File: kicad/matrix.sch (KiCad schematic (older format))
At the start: 19 parts, among them U1 TLC59025, U2 74HC595, U3 74HC595

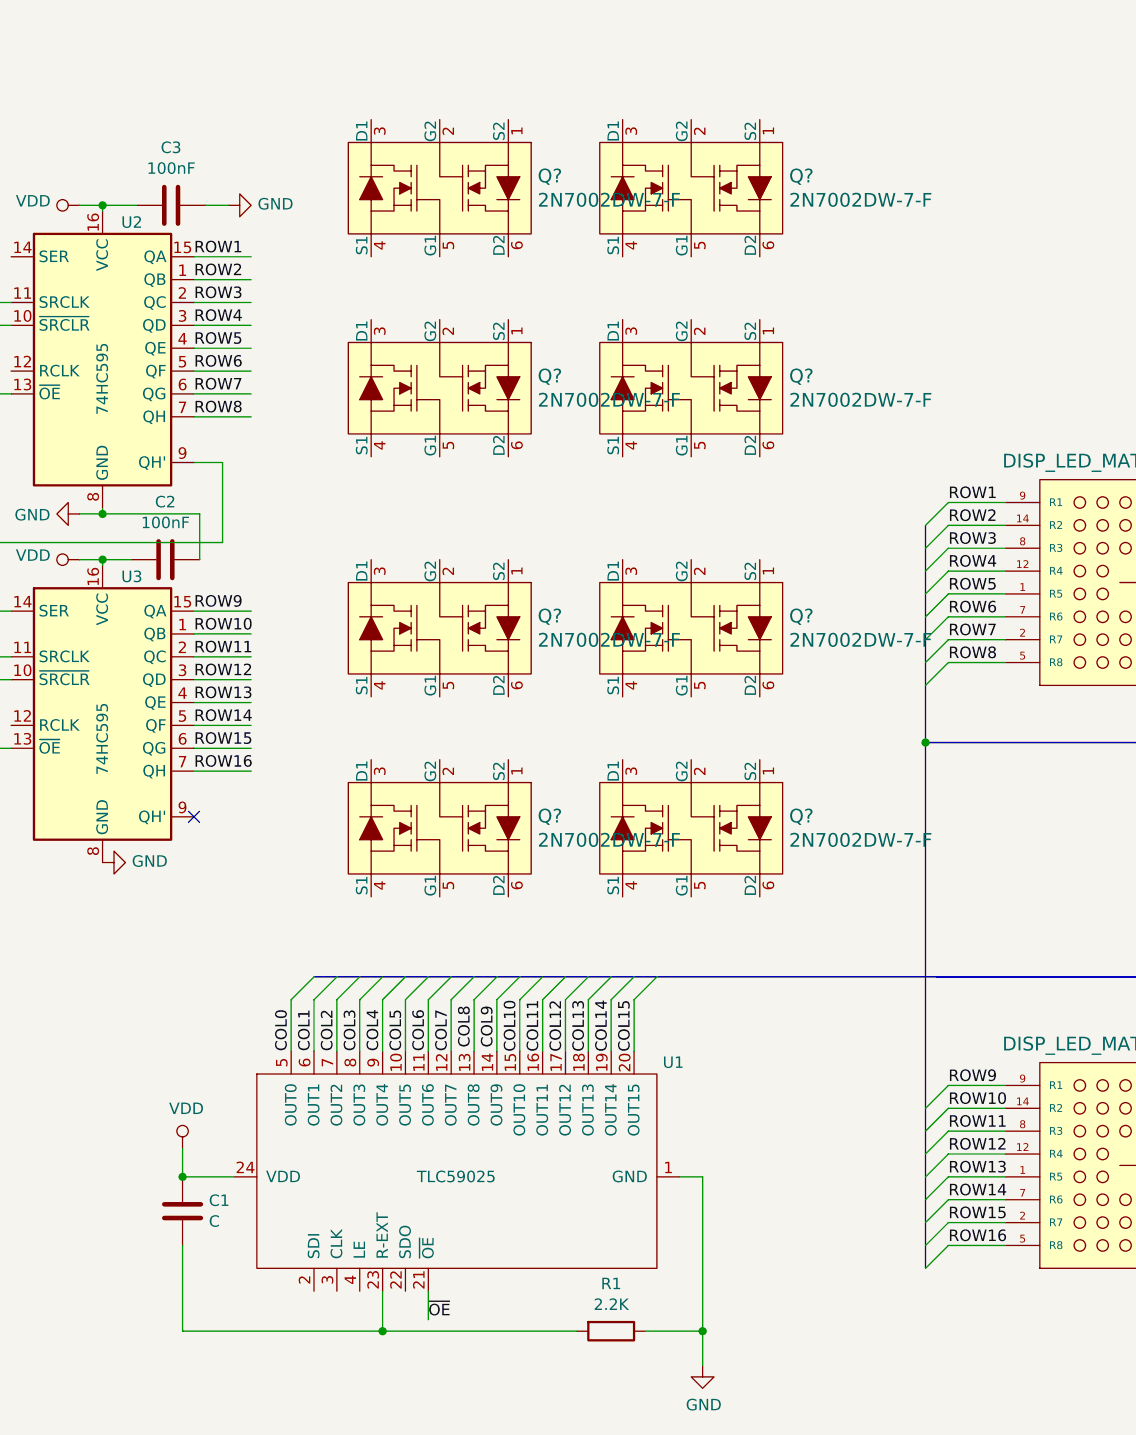
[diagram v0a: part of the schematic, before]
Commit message: Add footprints and initial layout
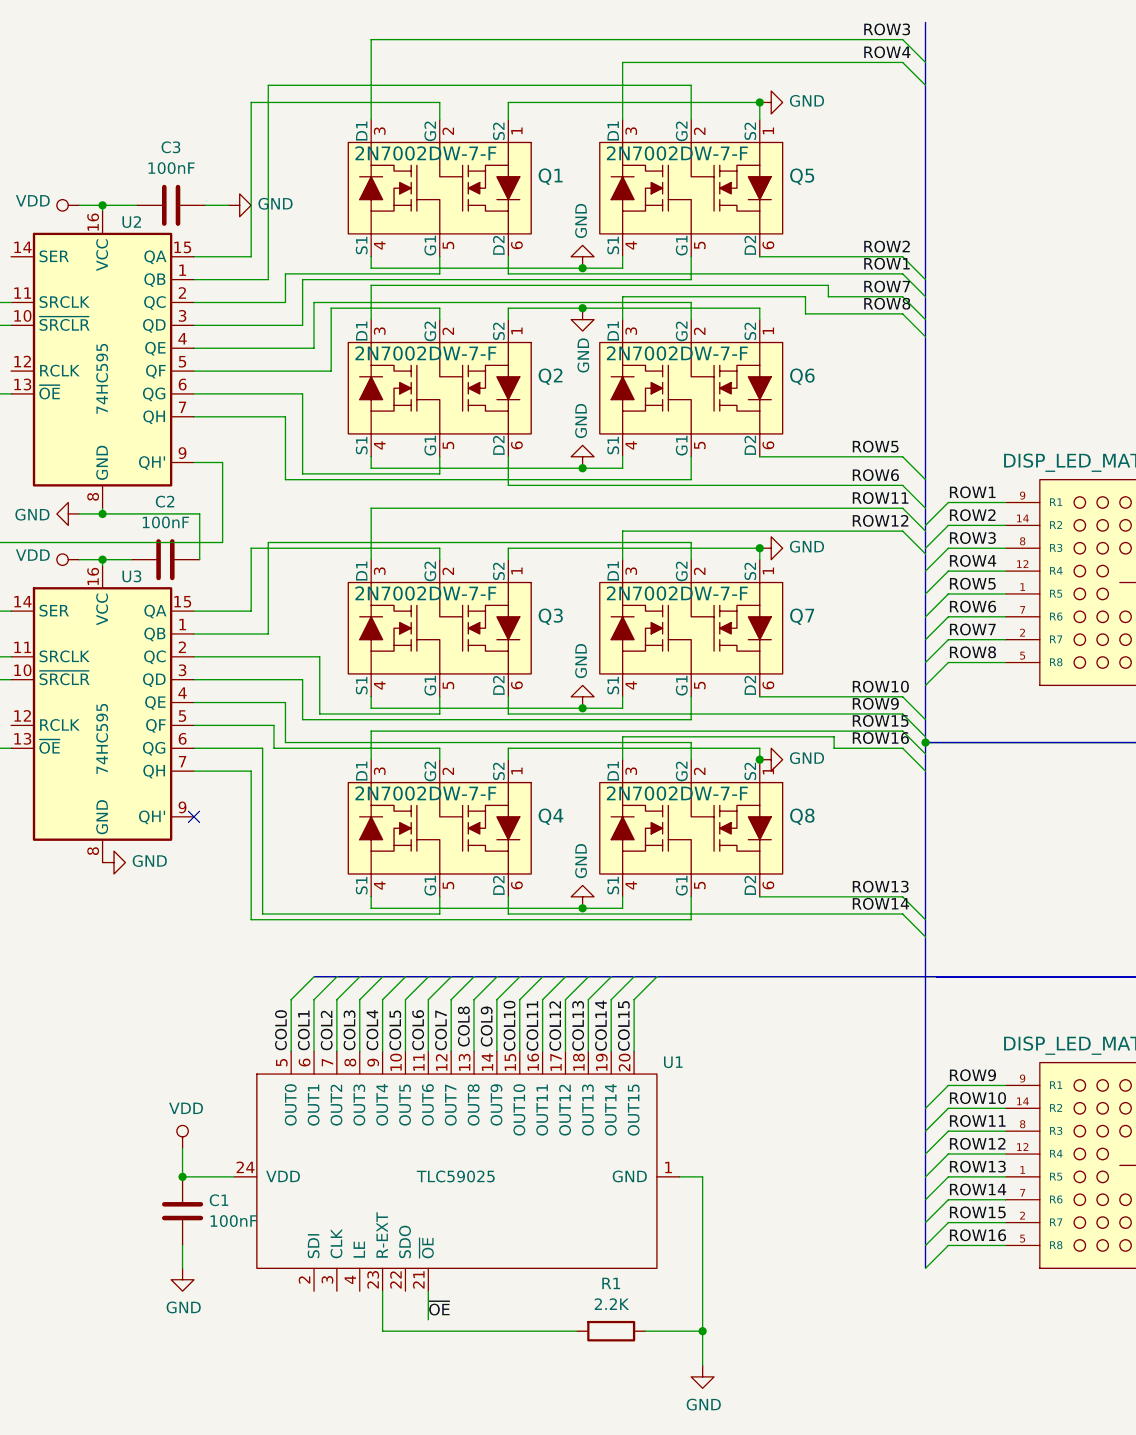
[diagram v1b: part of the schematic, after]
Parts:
- C1: value C -> 100nF; footprint (none) -> Capacitor_SMD:C_0805_2012Metric_Pad1.15x1.40mm_HandSolder
- C2, C3: footprint (none) -> Capacitor_SMD:C_0805_2012Metric_Pad1.15x1.40mm_HandSolder
- R1: footprint (none) -> Resistor_SMD:R_1206_3216Metric_Pad1.42x1.75mm_HandSolder
- gave numbers to parts that had none: 8
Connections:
- wire segments 132 -> 242

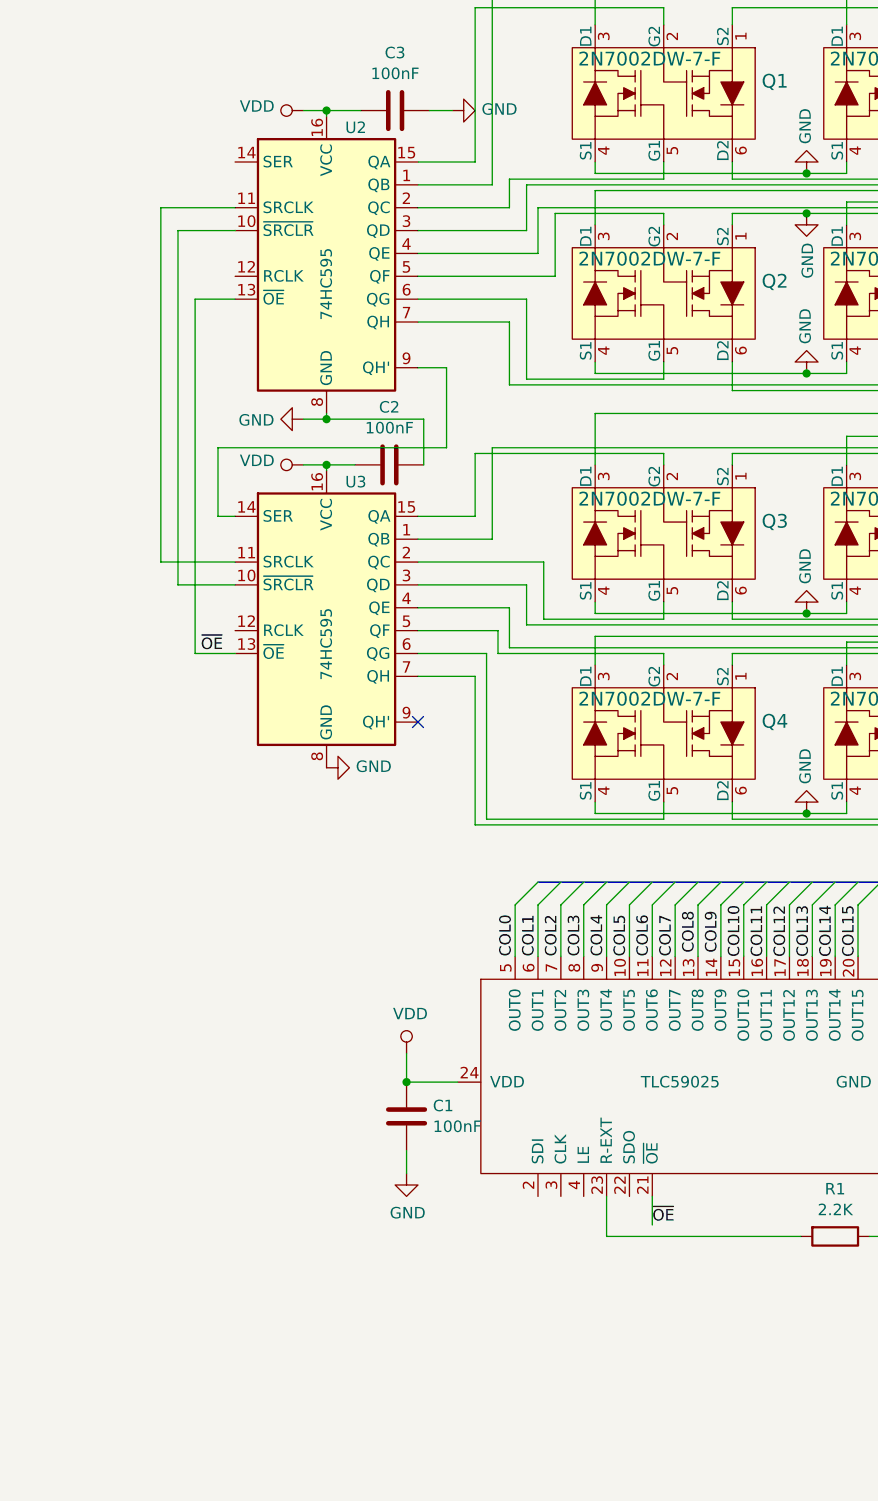
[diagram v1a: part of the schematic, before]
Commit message: Add headers to schematic
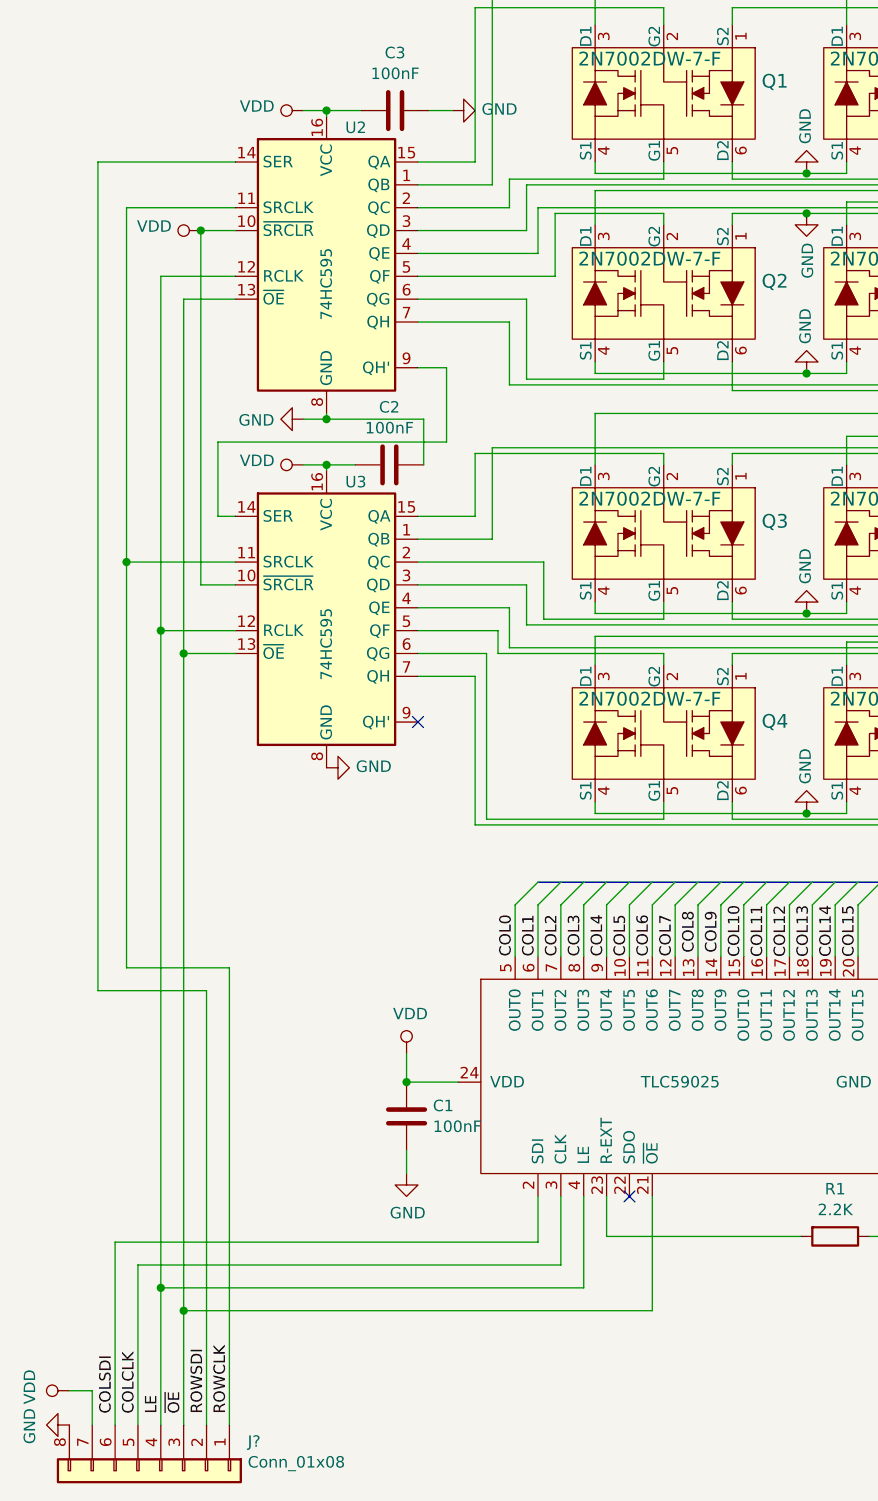
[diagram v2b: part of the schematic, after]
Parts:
- added J?: Conn_01x08, symbol Connector_Generic:Conn_01x08
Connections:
- net GND: now also J?.8 (Pin_8)
- net VDD: now also U2.10 (~SRCLR), U3.10 (~SRCLR), J?.7 (Pin_7)
- net ~OE: now also J?.3 (Pin_3)
- net COLSDI: now reaches U1.2 (SDI)
- net COLSDI: now also J?.6 (Pin_6)
- net COLCLK: now reaches U1.3 (CLK)
- net COLCLK: now also J?.5 (Pin_5)
- net LE: now reaches U1.4 (LE)
- net LE: now also U2.12 (RCLK), U3.12 (RCLK), J?.4 (Pin_4)
- net ROWCLK: now reaches U2.11 (SRCLK), U3.11 (SRCLK)
- net ROWCLK: now also J?.1 (Pin_1)
- net ROWSDI: now reaches U2.14 (SER)
- net ROWSDI: now also J?.2 (Pin_2)
- no-connect marks 1 -> 2
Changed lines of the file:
@@
 	2475 2650 2600 2650
 Wire Wire Line
-	2600 2650 2600 3000
-Wire Wire Line
-	2600 3000 1600 3000
-Wire Wire Line
-	1600 3000 1600 3300
+	2600 2650 2600 2975
+Wire Wire Line
+	2600 2975 1600 2975
+Wire Wire Line
+	1600 2975 1600 3300
 Wire Wire Line
 	1600 3300 1675 3300
@@
 $EndComp
 Wire Wire Line
-	1675 2350 1500 2350
-Wire Wire Line
-	1500 2350 1500 3900
-Wire Wire Line
-	1500 3900 1675 3900
-Wire Wire Line
-	1675 2050 1425 2050
-Wire Wire Line
-	1425 2050 1425 3600
-Wire Wire Line
-	1425 3600 1675 3600
-Wire Wire Line
-	1675 1950 1350 1950
-Wire Wire Line
-	1350 1950 1350 3500
-Wire Wire Line
-	1350 3500 1675 3500
+	1675 2350 1450 2350
+Wire Wire Line
+	1450 2350 1450 3900
+Wire Wire Line
+	1450 3900 1675 3900
+Wire Wire Line
+	1675 1950 1200 1950
+Wire Wire Line
+	1200 1950 1200 3500
+Wire Wire Line
+	1200 3500 1675 3500
 $Comp
 L power:VDD #PWR03
@@
 Wire Wire Line
 	2075 1525 2075 1550
-Text Label 1525 3900 0    50   ~ 0
+Text Label 1450 7225 1    50   ~ 0
 ~OE
-Text Label 3500 6400 0    50   ~ 0
-~OE
-Wire Wire Line
-	3500 6275 3500 6400
 Wire Wire Line
 	2475 1750 2725 1750
@@
 Wire Wire Line
 	4175 4600 4350 4600
-Wire Bus Line
-	8450 3875 8450 6175
-Wire Bus Line
-	8450 2925 8450 3875
-Wire Bus Line
-	10475 4900 10475 6175
-Wire Bus Line
-	10475 2925 10475 4900
-Wire Bus Line
-	7700 4900 7700 6175
-Wire Bus Line
-	7700 2925 7700 4900
-Wire Bus Line
-	5675 3875 5675 6175
-Wire Bus Line
-	3000 4900 7700 4900
-Wire Bus Line
-	5675 725  5675 3875
 $Comp
 L power:GND #PWR?
@@
 	1    0    0    -1
 $EndComp
+NoConn ~ 3400 6275
+$Comp
+L Connector_Generic:Conn_01x08 J?
+U 1 1 5EE0A62F
+P 1350 7475
+F 0 "J?" V 1222 7855 50  0000 L CNN
+F 1 "Conn_01x08" V 1313 7855 50  0000 L CNN
+F 2 "" H 1350 7475 50  0001 C CNN
+F 3 "~" H 1350 7475 50  0001 C CNN
+	1    1350 7475
+	0    1    1    0
+$EndComp
+$Comp
+L power:GND #PWR?
+U 1 1 5EE44BE5
+P 950 7275
+F 0 "#PWR?" H 950 7025 50  0001 C CNN
+F 1 "GND" H 955 7102 50  0000 C CNN
+F 2 "" H 950 7275 50  0001 C CNN
+F 3 "" H 950 7275 50  0001 C CNN
+	1    950  7275
+	0    1    1    0
+$EndComp
+$Comp
+L power:VDD #PWR?
+U 1 1 5EE456DF
+P 950 7125
+F 0 "#PWR?" H 950 6975 50  0001 C CNN
+F 1 "VDD" H 967 7298 50  0000 C CNN
+F 2 "" H 950 7125 50  0001 C CNN
+F 3 "" H 950 7125 50  0001 C CNN
+	1    950  7125
+	0    -1   -1   0
+$EndComp
+Wire Wire Line
+	950  7125 1050 7125
+Wire Wire Line
+	1050 7125 1050 7275
+Wire Wire Line
+	3000 6275 3000 6475
+Wire Wire Line
+	3000 6475 1150 6475
+Wire Wire Line
+	1150 6475 1150 7275
+Wire Wire Line
+	3100 6275 3100 6575
+Wire Wire Line
+	3100 6575 1250 6575
+Wire Wire Line
+	1250 6575 1250 7275
+Wire Wire Line
+	3200 6275 3200 6675
+Wire Wire Line
+	3200 6675 1350 6675
+Wire Wire Line
+	1350 6675 1350 7275
+Wire Wire Line
+	3500 6775 1450 6775
+Wire Wire Line
+	1450 6775 1450 7275
+Wire Wire Line
+	3500 6275 3500 6775
+Wire Wire Line
+	1450 3900 1450 6775
+Connection ~ 1450 3900
+Connection ~ 1450 6775
+Wire Wire Line
+	1675 1750 1075 1750
+Wire Wire Line
+	1075 1750 1075 5375
+Wire Wire Line
+	1075 5375 1550 5375
+Wire Wire Line
+	1550 5375 1550 7275
+$Comp
+L power:VDD #PWR?
+U 1 1 5EF45125
+P 1525 2050
+F 0 "#PWR?" H 1525 1900 50  0001 C CNN
+F 1 "VDD" V 1543 2177 50  0000 L CNN
+F 2 "" H 1525 2050 50  0001 C CNN
+F 3 "" H 1525 2050 50  0001 C CNN
+	1    1525 2050
+	0    -1   -1   0
+$EndComp
+Wire Wire Line
+	1525 3600 1525 2050
+Wire Wire Line
+	1525 2050 1675 2050
+Wire Wire Line
+	1525 3600 1675 3600
+Connection ~ 1525 2050
+Text Label 1150 7225 1    50   ~ 0
+COLSDI
+Text Label 1250 7225 1    50   ~ 0
+COLCLK
+Text Label 1350 7225 1    50   ~ 0
+LE
+Wire Wire Line
+	1350 6675 1350 3800
+Wire Wire Line
+	1350 3800 1675 3800
+Connection ~ 1350 6675
+Wire Wire Line
+	1350 3800 1350 2250
+Wire Wire Line
+	1350 2250 1675 2250
+Connection ~ 1350 3800
+Text Label 1550 7225 1    50   ~ 0
+ROWSDI
+Wire Wire Line
+	1200 3500 1200 5275
+Wire Wire Line
+	1200 5275 1650 5275
+Wire Wire Line
+	1650 5275 1650 7275
+Wire Bus Line
+	8450 3875 8450 6175
+Wire Bus Line
+	8450 2925 8450 3875
+Wire Bus Line
+	10475 4900 10475 6175
+Wire Bus Line
+	10475 2925 10475 4900
+Wire Bus Line
+	7700 4900 7700 6175
+Wire Bus Line
+	7700 2925 7700 4900
+Wire Bus Line
+	5675 3875 5675 6175
+Wire Bus Line
+	3000 4900 7700 4900
+Wire Bus Line
+	5675 725  5675 3875
+Connection ~ 1200 3500
+Text Label 1650 7225 1    50   ~ 0
+ROWCLK
 $EndSCHEMATC

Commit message: Add headers to PCB layout
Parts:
- J1: renamed from J?; footprint (none) -> Connector_PinHeader_2.54mm:PinHeader_1x08_P2.54mm_Horizontal
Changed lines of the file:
@@
 	4175 4600 4350 4600
 $Comp
-L power:GND #PWR?
+L power:GND #PWR019
 U 1 1 5F217EB1
 P 2425 6175
-F 0 "#PWR?" H 2425 5925 50  0001 C CNN
+F 0 "#PWR019" H 2425 5925 50  0001 C CNN
 F 1 "GND" H 2430 6002 50  0000 C CNN
 F 2 "" H 2425 6175 50  0001 C CNN
@@
 NoConn ~ 3400 6275
 $Comp
-L Connector_Generic:Conn_01x08 J?
+L Connector_Generic:Conn_01x08 J1
 U 1 1 5EE0A62F
 P 1350 7475
-F 0 "J?" V 1222 7855 50  0000 L CNN
+F 0 "J1" V 1222 7855 50  0000 L CNN
 F 1 "Conn_01x08" V 1313 7855 50  0000 L CNN
-F 2 "" H 1350 7475 50  0001 C CNN
+F 2 "Connector_PinHeader_2.54mm:PinHeader_1x08_P2.54mm_Horizontal" H 1350 7475 50  0001 C CNN
 F 3 "~" H 1350 7475 50  0001 C CNN
 	1    1350 7475
@@
 $EndComp
 $Comp
-L power:GND #PWR?
+L power:GND #PWR017
 U 1 1 5EE44BE5
 P 950 7275
-F 0 "#PWR?" H 950 7025 50  0001 C CNN
+F 0 "#PWR017" H 950 7025 50  0001 C CNN
 F 1 "GND" H 955 7102 50  0000 C CNN
 F 2 "" H 950 7275 50  0001 C CNN
@@
 $EndComp
 $Comp
-L power:VDD #PWR?
+L power:VDD #PWR016
 U 1 1 5EE456DF
 P 950 7125
-F 0 "#PWR?" H 950 6975 50  0001 C CNN
+F 0 "#PWR016" H 950 6975 50  0001 C CNN
 F 1 "VDD" H 967 7298 50  0000 C CNN
 F 2 "" H 950 7125 50  0001 C CNN
@@
 	1550 5375 1550 7275
 $Comp
-L power:VDD #PWR?
+L power:VDD #PWR018
 U 1 1 5EF45125
 P 1525 2050
-F 0 "#PWR?" H 1525 1900 50  0001 C CNN
+F 0 "#PWR018" H 1525 1900 50  0001 C CNN
 F 1 "VDD" V 1543 2177 50  0000 L CNN
 F 2 "" H 1525 2050 50  0001 C CNN
